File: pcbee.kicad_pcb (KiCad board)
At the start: 2 copper layers, 50.8 x 43.2 mm, 5 parts

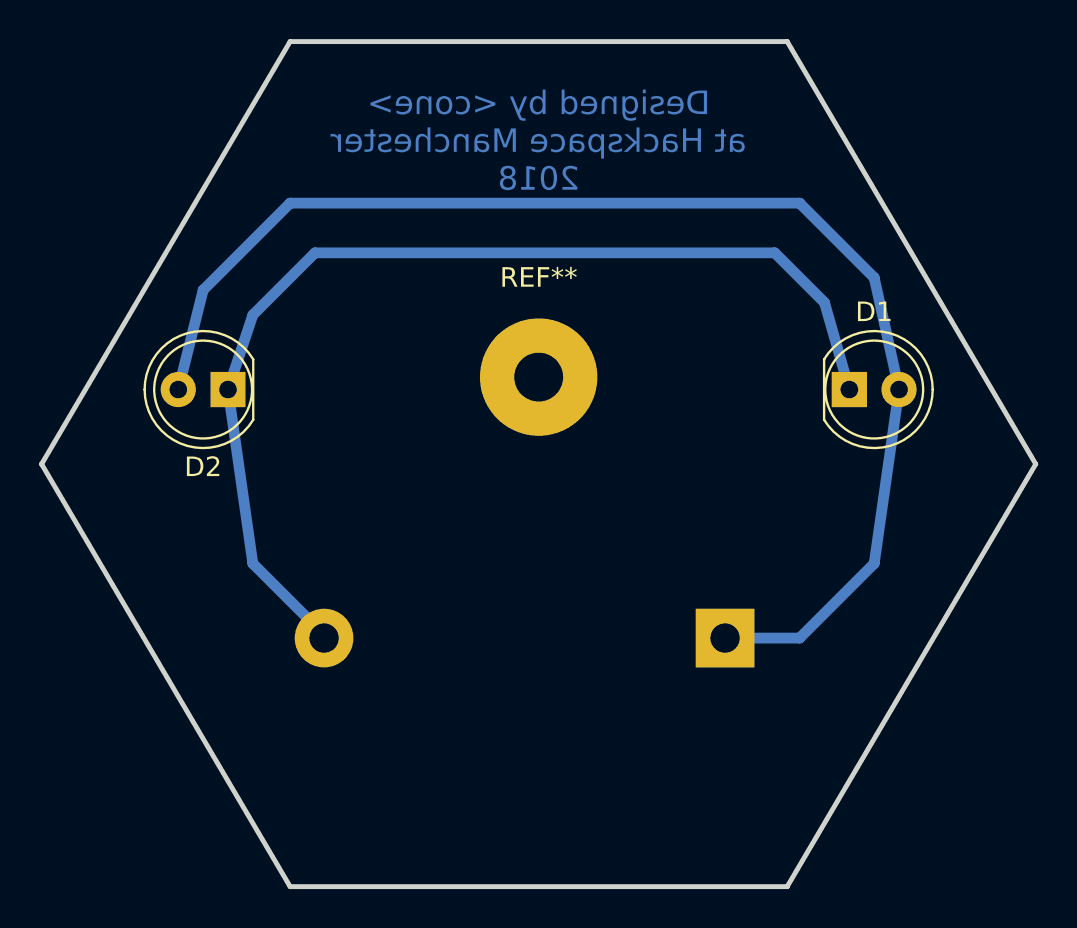
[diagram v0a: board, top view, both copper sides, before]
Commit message: I fixed it (#1)
* Fixed top fill, minor placement and routing changes.

Top fill redone to remove shorts.
Battery holder moved to prevent encroachment on design
This has resulted in the outline of the battery holder being over the pin, but as it is on the back and the battery holder has standoffs it should not interfere.

* Created gerbers

Created gerbers from latest commit.
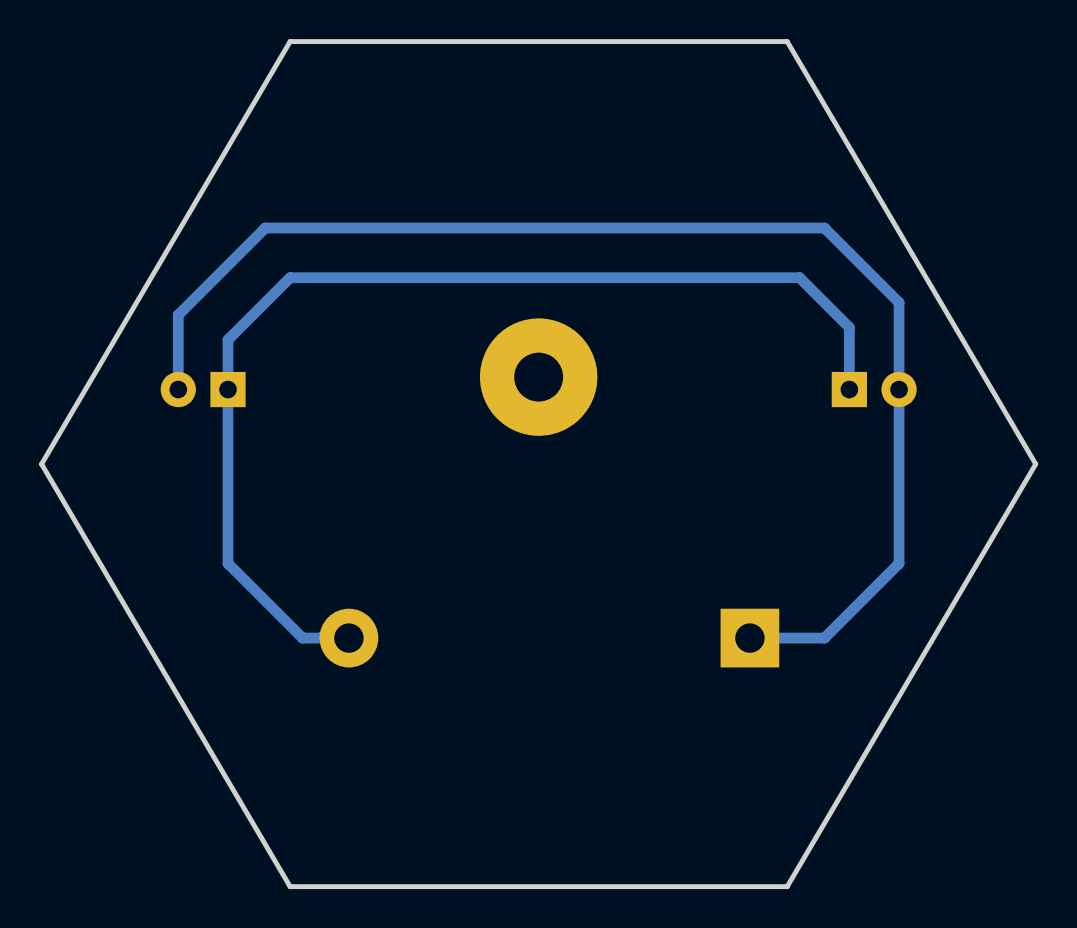
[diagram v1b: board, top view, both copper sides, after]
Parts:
- D1, D2: moved to B.Cu
- moved BT1 1.27 mm to (160.7, 105.4)
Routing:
- net Net-(BT1-Pad2): track 54.5 -> 56.7 mm

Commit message: Changed text to be degigned by committee
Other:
- board text added: "Designed by Committee at Hackspace Manchester 2018"
- board text removed: "Designed by <cone> at Hackspace Manchester 2018"
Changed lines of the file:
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@@
     (links 4)
     (no_connects 0)
-    (area 124.334999 74.804999 175.385001 118.235001)
+    (area 124.334999 74.804999 175.385001 119.485)
     (thickness 1.6)
     (drawings 7)
@@
     (34 B.Paste user hide)
     (35 F.Paste user)
-    (36 B.SilkS user hide)
+    (36 B.SilkS user)
     (37 F.SilkS user)
     (38 B.Mask user hide)
@@
     (pad 1 thru_hole circle (at 0 0) (size 5.99948 5.99948) (drill 2.49936) (layers *.Cu *.Mask))
   )
-  (gr_text "Designed by <cone>\nat Hackspace Manchester\n2018" (at 149.86 80.01) (layer B.SilkS)
+  (gr_text "Designed by Committee\nat Hackspace Manchester\n2018" (at 149.86 80.01) (layer B.SilkS)
     (effects (font (size 1.2 1.2) (thickness 0.3)) (justify mirror))
   )

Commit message: Generate gerbers
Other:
- board text added: "PRODUCTION ID MUST BE ON THIS (BACK) SILK"
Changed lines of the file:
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@@
     (area 124.334999 74.804999 175.385001 119.485)
     (thickness 1.6)
-    (drawings 7)
+    (drawings 8)
     (tracks 17)
     (zones 0)
@@
   (page A4)
   (layers
-    (0 F.Cu signal)
-    (31 B.Cu signal)
+    (0 F.Cu signal hide)
+    (31 B.Cu signal hide)
     (32 B.Adhes user hide)
     (33 F.Adhes user hide)
     (34 B.Paste user hide)
-    (35 F.Paste user)
-    (36 B.SilkS user)
-    (37 F.SilkS user)
+    (35 F.Paste user hide)
+    (36 B.SilkS user hide)
+    (37 F.SilkS user hide)
     (38 B.Mask user hide)
-    (39 F.Mask user)
+    (39 F.Mask user hide)
     (40 Dwgs.User user hide)
     (41 Cmts.User user hide)
@@
     (46 B.CrtYd user hide)
     (47 F.CrtYd user hide)
-    (48 B.Fab user hide)
-    (49 F.Fab user hide)
+    (48 B.Fab user)
+    (49 F.Fab user)
   )
   (setup
@@
     (pad_to_mask_clearance 0.2)
     (aux_axis_origin 0 0)
-    (visible_elements FFFFFF7F)
+    (visible_elements FFFF3F1F)
     (pcbplotparams
       (layerselection 0x010f0_80000001)
@@
     (pad 1 thru_hole circle (at 0 0) (size 5.99948 5.99948) (drill 2.49936) (layers *.Cu *.Mask))
   )
+  (gr_text "PRODUCTION ID\nMUST BE ON\nTHIS (BACK) SILK" (at 150.495 99.695) (layer B.Fab)
+    (effects (font (size 1.5 1.5) (thickness 0.3)))
+  )
   (gr_text "Designed by Committee\nat Hackspace Manchester\n2018" (at 149.86 80.01) (layer B.SilkS)
